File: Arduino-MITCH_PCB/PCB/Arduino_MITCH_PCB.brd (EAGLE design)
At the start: 63.5 x 112.7 mm, 9 parts, among them IC1 TC58CVG2S0HRAIJ, J1 1725656

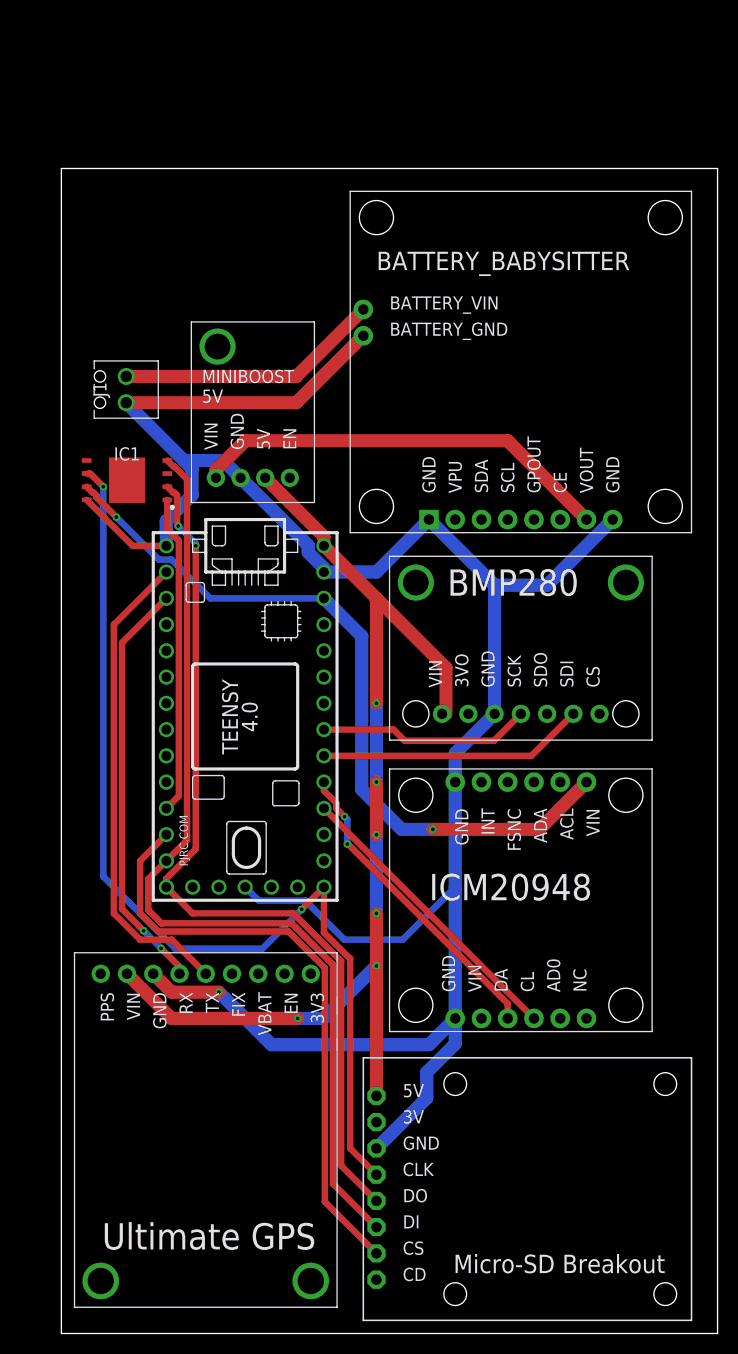
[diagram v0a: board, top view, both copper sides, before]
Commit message: Added a piezo buzzer to PCB
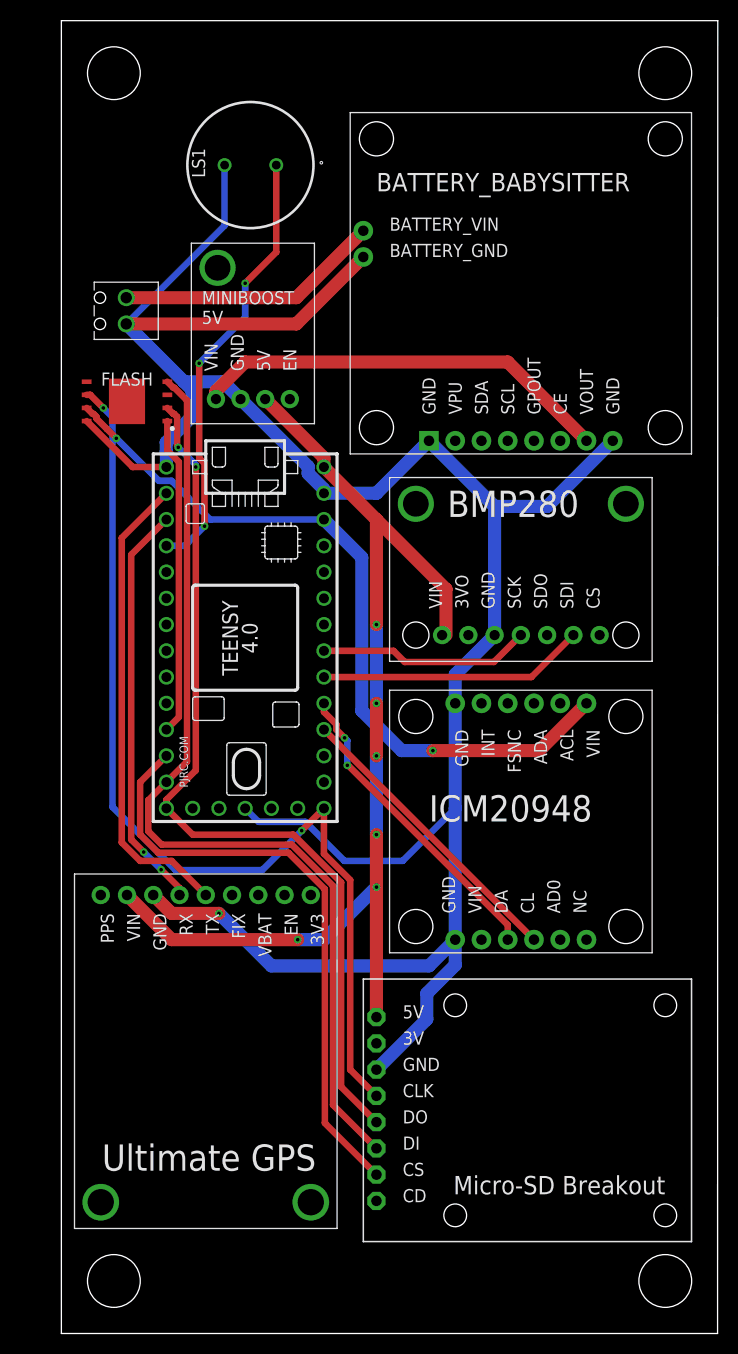
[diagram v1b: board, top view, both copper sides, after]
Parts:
- removed IC1: TC58CVG2S0HRAIJ, Arduino-MITCH_Breakouts:SON127P800X600X80-9N
- added FLASH: TC58CVG2S0HRAIJ, Arduino-MITCH_Breakouts:SON127P800X600X80-9N
- added LS1: PS1240P02BT, SamacSys_Parts:PS1240P02BT
- moved J1 7.62 mm to (3.17, 98.9)
- moved U$1 7.62 mm to (17.8, 67.3)
- moved U$2 7.62 mm to (26.7, 44.5)
- moved U$3 7.62 mm to (27.9, 85.1)
- moved U$5 7.62 mm to (61.0, 34.3)
- moved U$6 7.62 mm to (31.8, 36.8)
- moved U$7 7.62 mm to (31.8, 65.0)
- moved U$4 7.62 mm to (12.6, 88.0)
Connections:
- new net BUZZ: LS1.1, U$1.2
- net 3V3: now also FLASH.7; no longer IC1.7
- net CS2: now also FLASH.1; no longer IC1.1
- net GND: now also FLASH.8, LS1.2; no longer IC1.8
- net MISO: now also FLASH.2; no longer IC1.2
- net MOSI: now also FLASH.4; no longer IC1.4
- net SCK: now also FLASH.6; no longer IC1.6
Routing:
- net BUZZ: track 0.00 -> 42.7 mm, vias 0 -> 3
- net GND: track 223.5 -> 242.8 mm
- net RX1: track 40.4 -> 39.7 mm
- net TX1: track 46.4 -> 45.8 mm
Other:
- board size 63.5 x 112.7 mm -> 63.5 x 127 mm

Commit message: Added LED for debugging and custom images
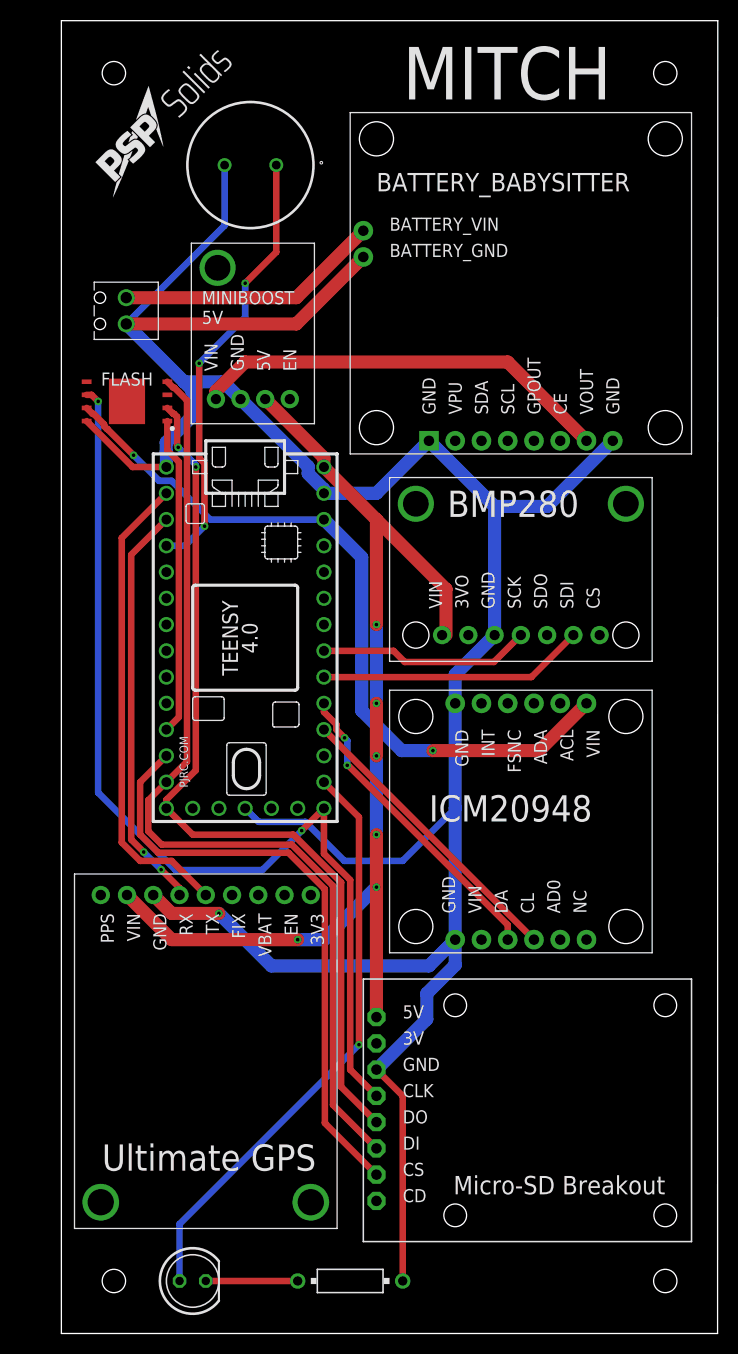
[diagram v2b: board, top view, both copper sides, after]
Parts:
- added LED1: RED, led:LED5MM
- added R1: 560, resistor-power:HPS58
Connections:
- new net LED: LED1.A, U$1.14/A0
- new net LED-RES: LED1.K, R1.1
- net GND: now also R1.2
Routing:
- net LED: track 0.00 -> 56.9 mm, vias 0 -> 1
- net GND: track 242.8 -> 264.3 mm
- net LED-RES: track 0.00 -> 8.89 mm
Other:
- board text added: "MITCH"
